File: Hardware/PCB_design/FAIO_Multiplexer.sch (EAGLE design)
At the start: 9 parts, among them J1 SJ1-3535NG, J2 SJ1-3535NG, J3 SJ1-3535NG, J4 SJ1-3535NG

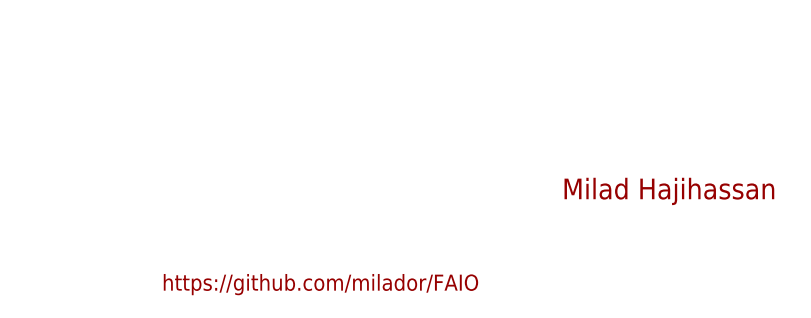
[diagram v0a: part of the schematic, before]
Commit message: Changed FAIO project github page to two separate projects
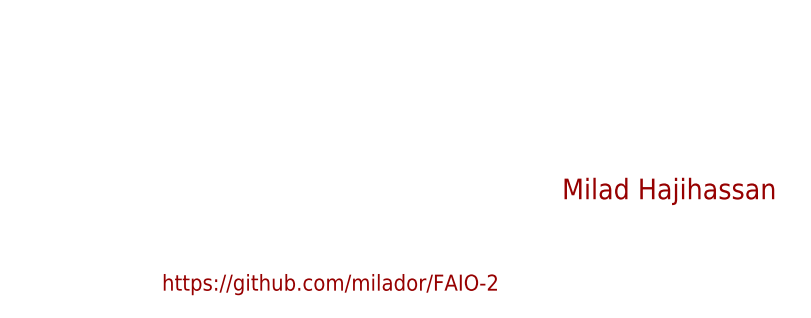
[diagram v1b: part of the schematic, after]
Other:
- note added: "https://github.com/milador/FAIO-2"
- note removed: "https://github.com/milador/FAIO"
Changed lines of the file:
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@@
 <sheet>
 <plain>
-<text x="93.98" y="-55.88" size="1.778" layer="94">https://github.com/milador/FAIO</text>
+<text x="93.98" y="-55.88" size="1.778" layer="94">https://github.com/milador/FAIO-2</text>
 <text x="138.43" y="-45.72" size="2.286" layer="94">Milad Hajihassan</text>
 </plain>

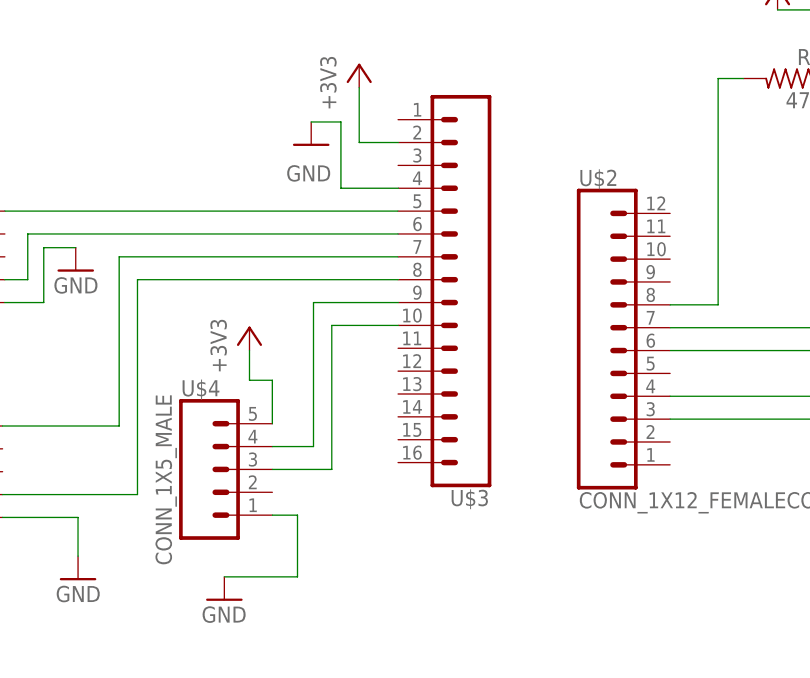
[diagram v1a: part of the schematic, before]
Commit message: Updated PCB Files: 2.0 text changed to Multiplexer
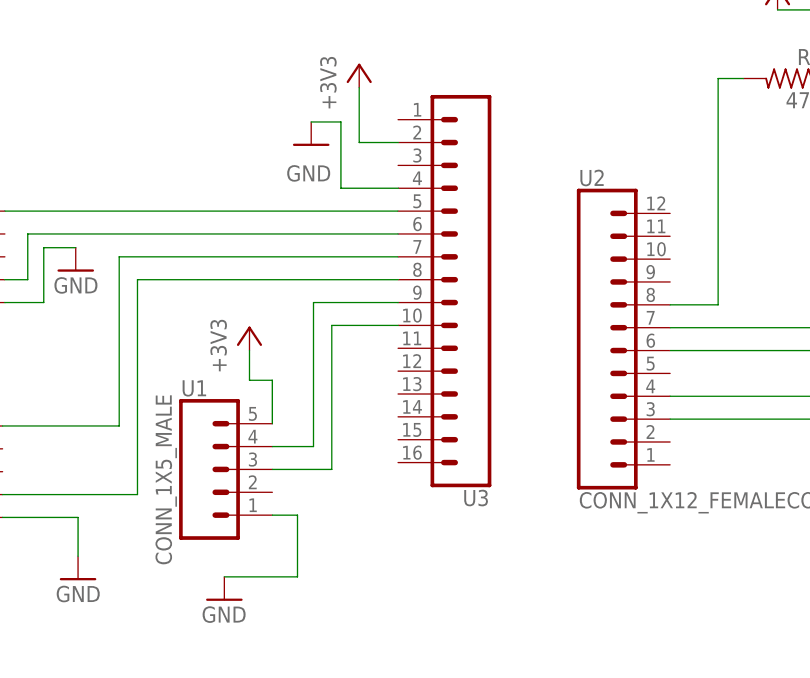
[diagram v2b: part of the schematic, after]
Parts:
- renumbered U$2 to U2, U$3 to U3, U$4 to U1
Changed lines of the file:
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@@
 <?xml version="1.0" encoding="utf-8"?>
 <!DOCTYPE eagle SYSTEM "eagle.dtd">
-<eagle version="9.3.0">
+<eagle version="9.6.2">
 <drawing>
 <settings>
@@
 <part name="GND1" library="SparkFun-Aesthetics" deviceset="GND" device=""/>
 <part name="LED1" library="milador" library_urn="urn:adsk.eagle:library:7092934" deviceset="NEOPIXELS-5MM" device="" package3d_urn="urn:adsk.eagle:package:6677832/4" value="LED"/>
-<part name="U$2" library="milador" library_urn="urn:adsk.eagle:library:7092934" deviceset="CONN_1X12_FEMALE" device="CONN_1X12_FEMALE" package3d_urn="urn:adsk.eagle:package:6686451/2" value="CONN_1X12_FEMALECONN_1X12_FEMALE"/>
-<part name="U$3" library="milador" library_urn="urn:adsk.eagle:library:7092934" deviceset="CONN_1X16_FEMALE" device="CONN_1X16_FEMALE" package3d_urn="urn:adsk.eagle:package:6686444/2" value=""/>
-<part name="U$4" library="milador" library_urn="urn:adsk.eagle:library:7092934" deviceset="CONN_1X5_MALE" device="" package3d_urn="urn:adsk.eagle:package:6908637/1"/>
+<part name="U2" library="milador" library_urn="urn:adsk.eagle:library:7092934" deviceset="CONN_1X12_FEMALE" device="CONN_1X12_FEMALE" package3d_urn="urn:adsk.eagle:package:6686451/2" value="CONN_1X12_FEMALECONN_1X12_FEMALE"/>
+<part name="U3" library="milador" library_urn="urn:adsk.eagle:library:7092934" deviceset="CONN_1X16_FEMALE" device="CONN_1X16_FEMALE" package3d_urn="urn:adsk.eagle:package:6686444/2" value=""/>
+<part name="U1" library="milador" library_urn="urn:adsk.eagle:library:7092934" deviceset="CONN_1X5_MALE" device="" package3d_urn="urn:adsk.eagle:package:6908637/1"/>
 <part name="+3V2" library="supply1" library_urn="urn:adsk.eagle:library:371" deviceset="+3V3" device=""/>
 <part name="GND6" library="SparkFun-Aesthetics" deviceset="GND" device=""/>
@@
 <attribute name="VALUE" x="100.076" y="75.946" size="1.778" layer="95" font="vector" align="bottom-center"/>
 </instance>
-<instance part="U$2" gate="G$1" x="52.578" y="53.34" smashed="yes">
+<instance part="U2" gate="G$1" x="52.578" y="53.34" smashed="yes">
 <attribute name="VALUE" x="52.578" y="33.274" size="1.778" layer="96" font="vector"/>
 <attribute name="NAME" x="52.578" y="69.088" size="1.778" layer="95" font="vector"/>
 </instance>
-<instance part="U$3" gate="G$1" x="42.672" y="56.134" smashed="yes" rot="R180">
+<instance part="U3" gate="G$1" x="42.672" y="56.134" smashed="yes" rot="R180">
 <attribute name="VALUE" x="42.672" y="81.28" size="1.778" layer="96" font="vector" rot="R180"/>
 <attribute name="NAME" x="42.672" y="35.306" size="1.778" layer="95" font="vector" rot="R180"/>
 </instance>
-<instance part="U$4" gate="G$1" x="10.922" y="37.592" smashed="yes">
+<instance part="U1" gate="G$1" x="10.922" y="37.592" smashed="yes">
 <attribute name="VALUE" x="7.366" y="26.924" size="1.778" layer="96" font="vector" rot="R90"/>
 <attribute name="NAME" x="8.382" y="45.72" size="1.778" layer="95" font="vector"/>
@@
 <wire x1="26.162" y1="68.834" x2="26.162" y2="76.2" width="0.1524" layer="91"/>
 <wire x1="26.162" y1="76.2" x2="22.86" y2="76.2" width="0.1524" layer="91"/>
-<pinref part="U$3" gate="G$1" pin="4"/>
+<pinref part="U3" gate="G$1" pin="4"/>
 <wire x1="32.512" y1="68.834" x2="26.162" y2="68.834" width="0.1524" layer="91"/>
 </segment>
@@
 <wire x1="13.208" y1="25.654" x2="21.336" y2="25.654" width="0.1524" layer="91"/>
 <wire x1="21.336" y1="25.654" x2="21.336" y2="32.512" width="0.1524" layer="91"/>
-<pinref part="U$4" gate="G$1" pin="1"/>
+<pinref part="U1" gate="G$1" pin="1"/>
 <wire x1="21.336" y1="32.512" x2="18.542" y2="32.512" width="0.1524" layer="91"/>
 </segment>
@@
 <pinref part="+3V1" gate="G$1" pin="+3V3"/>
 <wire x1="28.194" y1="73.914" x2="28.194" y2="80.01" width="0.1524" layer="91"/>
-<pinref part="U$3" gate="G$1" pin="2"/>
+<pinref part="U3" gate="G$1" pin="2"/>
 <wire x1="32.512" y1="73.914" x2="28.194" y2="73.914" width="0.1524" layer="91"/>
 </segment>
@@
 </segment>
 <segment>
-<pinref part="U$4" gate="G$1" pin="5"/>
+<pinref part="U1" gate="G$1" pin="5"/>
 <wire x1="18.542" y1="42.672" x2="18.542" y2="47.498" width="0.1524" layer="91"/>
 <pinref part="+3V2" gate="G$1" pin="+3V3"/>
@@
 <wire x1="80.264" y1="26.67" x2="80.264" y2="43.18" width="0.1524" layer="91"/>
 <wire x1="80.264" y1="43.18" x2="62.738" y2="43.18" width="0.1524" layer="91"/>
-<pinref part="U$2" gate="G$1" pin="3"/>
+<pinref part="U2" gate="G$1" pin="3"/>
 </segment>
 </net>
@@
 <net name="N$13" class="0">
 <segment>
-<pinref part="U$4" gate="G$1" pin="3"/>
+<pinref part="U1" gate="G$1" pin="3"/>
 <wire x1="18.542" y1="37.592" x2="25.146" y2="37.592" width="0.1524" layer="91"/>
 <wire x1="25.146" y1="37.592" x2="25.146" y2="53.594" width="0.1524" layer="91"/>
-<pinref part="U$3" gate="G$1" pin="10"/>
+<pinref part="U3" gate="G$1" pin="10"/>
 <wire x1="25.146" y1="53.594" x2="32.512" y2="53.594" width="0.1524" layer="91"/>
 </segment>
@@
 <net name="N$7" class="0">
 <segment>
-<pinref part="U$3" gate="G$1" pin="9"/>
+<pinref part="U3" gate="G$1" pin="9"/>
 <wire x1="32.512" y1="56.134" x2="23.114" y2="56.134" width="0.1524" layer="91"/>
 <wire x1="23.114" y1="56.134" x2="23.114" y2="40.132" width="0.1524" layer="91"/>
-<pinref part="U$4" gate="G$1" pin="4"/>
+<pinref part="U1" gate="G$1" pin="4"/>
 <wire x1="23.114" y1="40.132" x2="18.542" y2="40.132" width="0.1524" layer="91"/>
 </segment>
@@
 <net name="N$9" class="0">
 <segment>
-<pinref part="U$3" gate="G$1" pin="5"/>
+<pinref part="U3" gate="G$1" pin="5"/>
 <wire x1="32.512" y1="66.294" x2="-11.176" y2="66.294" width="0.1524" layer="91"/>
 <pinref part="J1" gate="G$1" pin="2"/>
@@
 <net name="N$10" class="0">
 <segment>
-<pinref part="U$3" gate="G$1" pin="6"/>
+<pinref part="U3" gate="G$1" pin="6"/>
 <wire x1="32.512" y1="63.754" x2="-8.636" y2="63.754" width="0.1524" layer="91"/>
 <pinref part="J1" gate="G$1" pin="3"/>
@@
 <wire x1="-11.43" y1="42.418" x2="1.524" y2="42.418" width="0.1524" layer="91"/>
 <wire x1="1.524" y1="42.418" x2="1.524" y2="61.214" width="0.1524" layer="91"/>
-<pinref part="U$3" gate="G$1" pin="7"/>
+<pinref part="U3" gate="G$1" pin="7"/>
 <wire x1="1.524" y1="61.214" x2="32.512" y2="61.214" width="0.1524" layer="91"/>
 </segment>
@@
 <wire x1="-11.43" y1="34.798" x2="3.556" y2="34.798" width="0.1524" layer="91"/>
 <wire x1="3.556" y1="34.798" x2="3.556" y2="58.674" width="0.1524" layer="91"/>
-<pinref part="U$3" gate="G$1" pin="8"/>
+<pinref part="U3" gate="G$1" pin="8"/>
 <wire x1="3.556" y1="58.674" x2="32.512" y2="58.674" width="0.1524" layer="91"/>
 </segment>
@@
 <net name="N$3" class="0">
 <segment>
-<pinref part="U$2" gate="G$1" pin="4"/>
+<pinref part="U2" gate="G$1" pin="4"/>
 <wire x1="62.738" y1="45.72" x2="82.55" y2="45.72" width="0.1524" layer="91"/>
 <wire x1="82.55" y1="45.72" x2="82.55" y2="34.29" width="0.1524" layer="91"/>
@@
 <net name="N$1" class="0">
 <segment>
-<pinref part="U$2" gate="G$1" pin="6"/>
+<pinref part="U2" gate="G$1" pin="6"/>
 <pinref part="J3" gate="G$1" pin="3"/>
 <wire x1="62.738" y1="50.8" x2="95.758" y2="50.8" width="0.1524" layer="91"/>
@@
 <wire x1="95.758" y1="58.42" x2="90.678" y2="58.42" width="0.1524" layer="91"/>
 <wire x1="90.678" y1="58.42" x2="90.678" y2="53.34" width="0.1524" layer="91"/>
-<pinref part="U$2" gate="G$1" pin="7"/>
+<pinref part="U2" gate="G$1" pin="7"/>
 <wire x1="90.678" y1="53.34" x2="62.738" y2="53.34" width="0.1524" layer="91"/>
 </segment>
@@
 <wire x1="70.866" y1="81.026" x2="68.072" y2="81.026" width="0.1524" layer="91"/>
 <wire x1="68.072" y1="81.026" x2="68.072" y2="55.88" width="0.1524" layer="91"/>
-<pinref part="U$2" gate="G$1" pin="8"/>
+<pinref part="U2" gate="G$1" pin="8"/>
 <wire x1="68.072" y1="55.88" x2="62.738" y2="55.88" width="0.1524" layer="91"/>
 </segment>
